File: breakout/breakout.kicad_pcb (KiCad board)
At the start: 2 copper layers, 3 parts, among them J101 scope, J102 pod_0-7, J103 pod_8-15

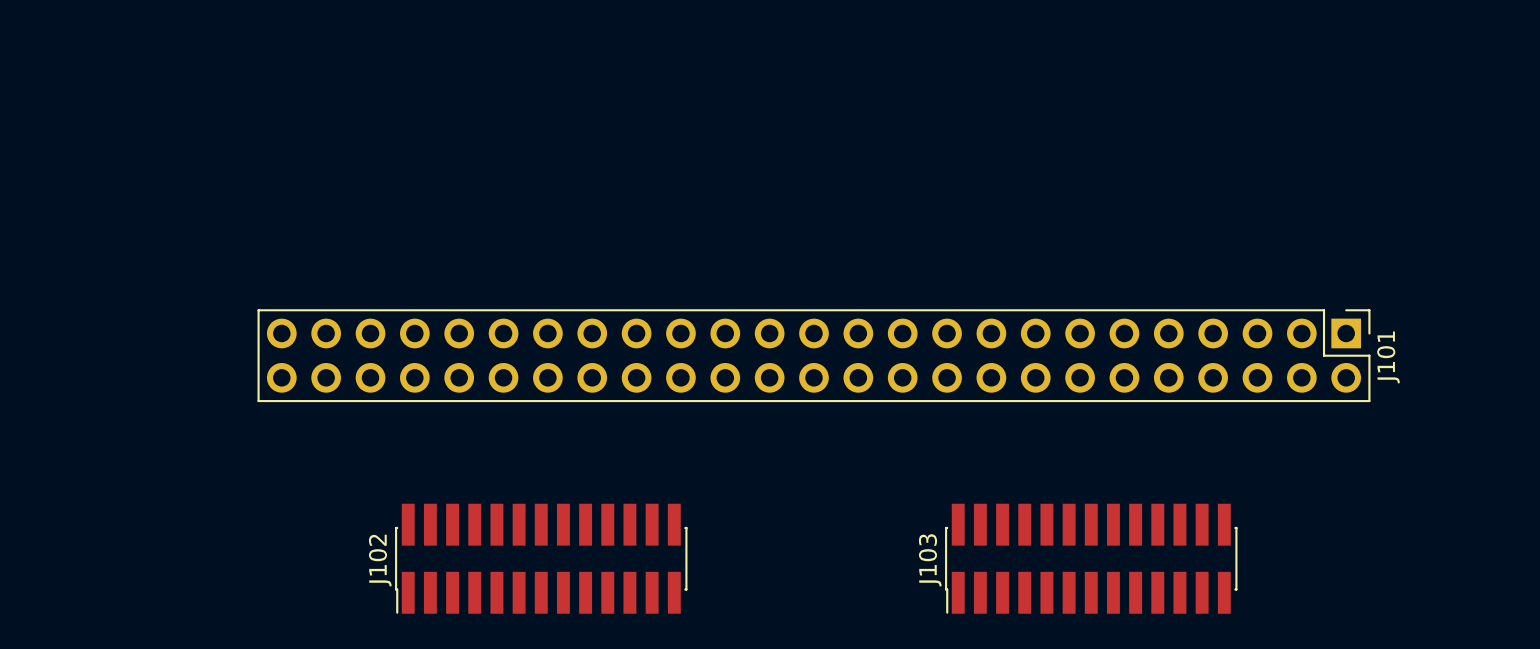
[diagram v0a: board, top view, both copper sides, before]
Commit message: Laid out 4 layer breakout board
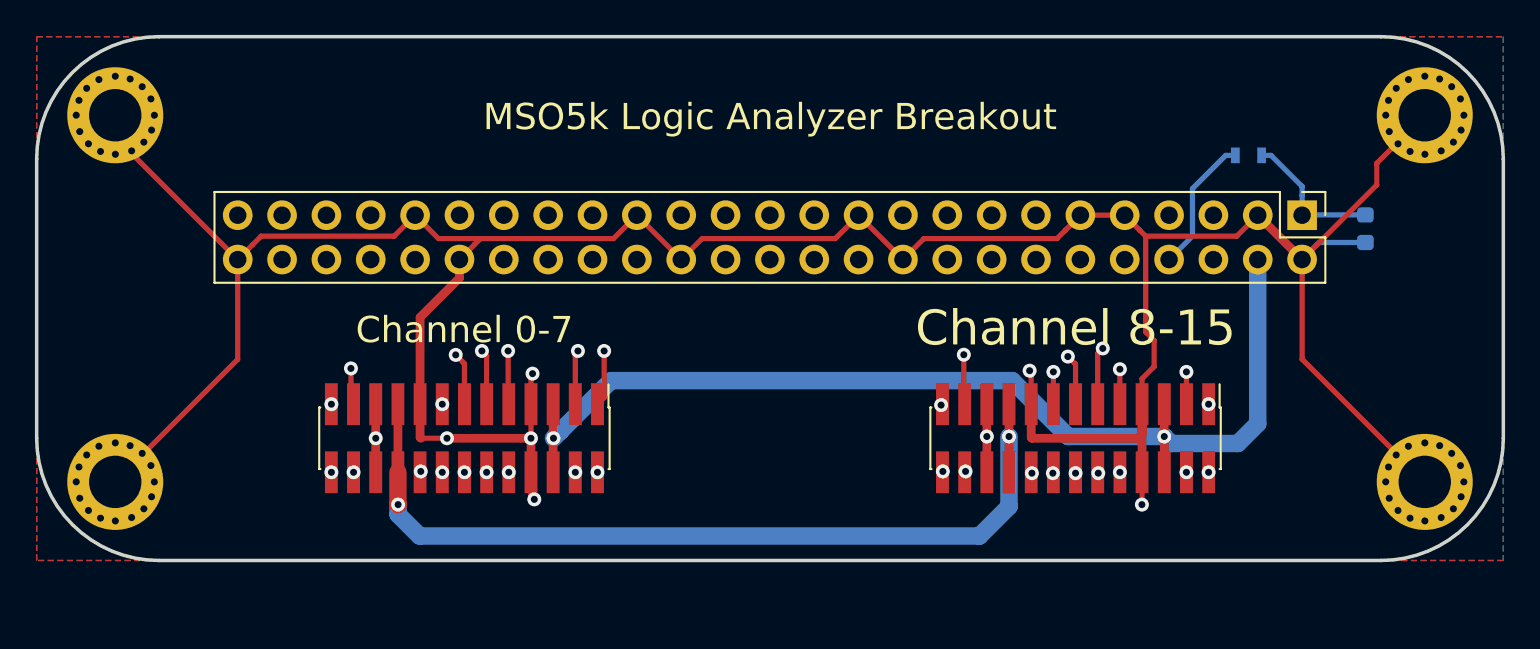
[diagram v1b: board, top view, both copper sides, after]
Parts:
- added J104: 3mm hole, projectdir:3mm, F.Cu at (58.5, 25.0)
- added J105: 3mm hole, projectdir:3mm, F.Cu at (58.5, 46.0)
- added J106: 3mm hole, projectdir:3mm, F.Cu at (133.5, 25.0)
- added J107: 3mm hole, projectdir:3mm, F.Cu at (133.5, 46.0)
- added R101: NF, Resistors_SMD.pretty:R_0603, B.Cu at (123.4, 27.3)
- added R102: 0, Resistor_SMD:R_0603_1608Metric, B.Cu at (130.1, 31.5)
- moved J102 8.18 mm to (78.5, 43.5), turned to 270 degrees
- moved J101 7.23 mm to (126.5, 30.7)
- moved J103 6.96 mm to (113.5, 43.5), turned to 270 degrees
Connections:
- J101 pad 1: GND -> Detect
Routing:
- net GND: track 0.00 -> 181.4 mm, vias 0 -> 6
- net +2V5: track 0.00 -> 90.1 mm, vias 0 -> 2
- net +4V: track 0.00 -> 79.0 mm, vias 0 -> 2
- net Vref_0-7: track 0.00 -> 65.2 mm, vias 0 -> 1
- net -2V5: track 0.00 -> 60.9 mm, vias 0 -> 2
- net D14+: track 0.00 -> 43.5 mm, vias 0 -> 1
- net D15+: track 0.00 -> 42.8 mm, vias 0 -> 1
- net D12+: track 0.00 -> 39.1 mm, vias 0 -> 1
- net D13+: track 0.00 -> 37.8 mm, vias 0 -> 1
- net D14-: track 0.00 -> 36.5 mm, vias 0 -> 1
- net D15-: track 0.00 -> 36.2 mm, vias 0 -> 1
- net D0+: track 0.00 -> 34.5 mm, vias 0 -> 1
- net D1+: track 0.00 -> 34.1 mm, vias 0 -> 1
- net Vref_8-15: track 0.00 -> 31.0 mm, vias 0 -> 1
- net D13-: track 0.00 -> 30.9 mm, vias 0 -> 1
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- added copper zone on B.Cu, net GND
- added copper zone on F.Cu, net GND
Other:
- board outline added: 84 x 30 mm
- copper layers 2 -> 4
- board text added: "Channel 0-7"
- board text added: "Channel 8-15"
- board text added: "MSO5k Logic Analyzer Breakout"

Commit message: Switched to 0805 on the pod for the large bulk caps
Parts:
- added G***: LOGO, breakout:qrcode, F.Cu at (95.8, 43.3)
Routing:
- net GND: track 181.4 -> 277.4 mm, vias 6 -> 8
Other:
- board text added: "This side towards scope. https://dren.dk https://gitlab.com/dren.dk/mso5k-la-pod 2018-01-30"

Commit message: Added proper readme
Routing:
- net +2V5: track 90.1 -> 102.4 mm
- net D15-: track 36.2 -> 47.2 mm
- net D2-: track 20.2 -> 30.3 mm
- net D14-: track 36.5 -> 45.9 mm
- net D4-: track 11.4 -> 20.6 mm
- net D7-: track 11.6 -> 19.9 mm
- net D6-: track 8.93 -> 17.1 mm
- net D9-: track 13.5 -> 21.6 mm
- net D12-: track 30.1 -> 37.9 mm
- net D13-: track 30.9 -> 38.6 mm
- net D8-: track 14.2 -> 21.8 mm
- net D11-: track 22.1 -> 29.5 mm
- net D0-: track 28.3 -> 35.4 mm
- net D10-: track 21.3 -> 28.1 mm
- net D5-: track 10.8 -> 16.6 mm
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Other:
- net class Default: clearance 0.2 -> 0.15
- rule trace_clearance: 0.2 -> 0.15
- rule trace_min: 0.2 -> 0.15
- board text added: "FRONT TOWARD SCOPE https://dren.dk https://gitlab.com/dren.dk/mso5k-la-pod 2018-02-03"
- board text removed: "This side towards scope. https://dren.dk https://gitlab.com/dren.dk/mso5k-la-pod 2018-01-30"

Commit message: Cleaning up
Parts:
- removed G***: LOGO, breakout:qrcode
- removed R101: NF, Resistors_SMD.pretty:R_0603
- removed R102: 0, Resistor_SMD:R_0603_1608Metric
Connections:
- J101 pad 1: Detect -> GND
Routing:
- net Detect: track 8.34 -> 0.00 mm
- net +4V: track 77.1 -> 69.3 mm
- net GND: track 277.1 -> 275.7 mm
